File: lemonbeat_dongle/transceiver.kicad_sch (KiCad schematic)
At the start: 21 parts, among them J301 SMA, U301 Si4467, Y301 26MHz

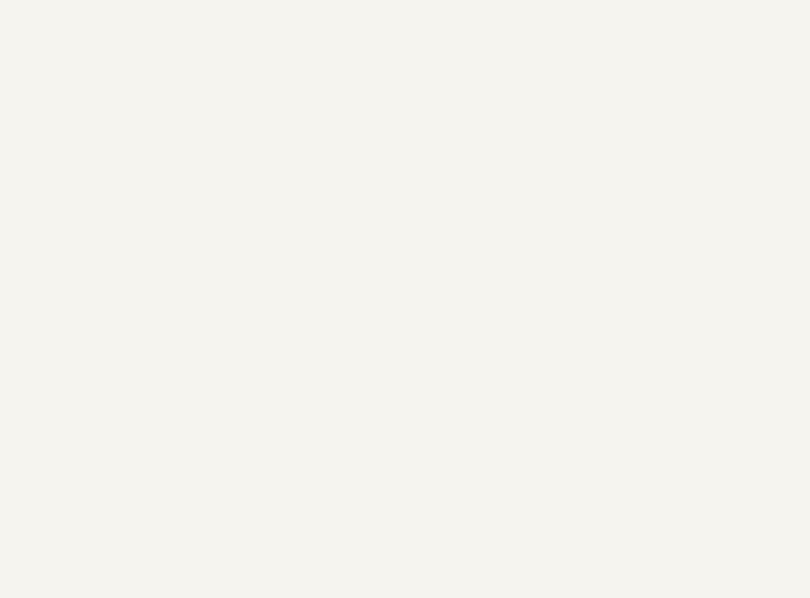
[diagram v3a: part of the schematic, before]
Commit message: dongle: add some LEDs
- power LED (connected to VBUS, constantly on if USB is powered)
- TX LED (GPIO2)
- RX LED (GPIO3)
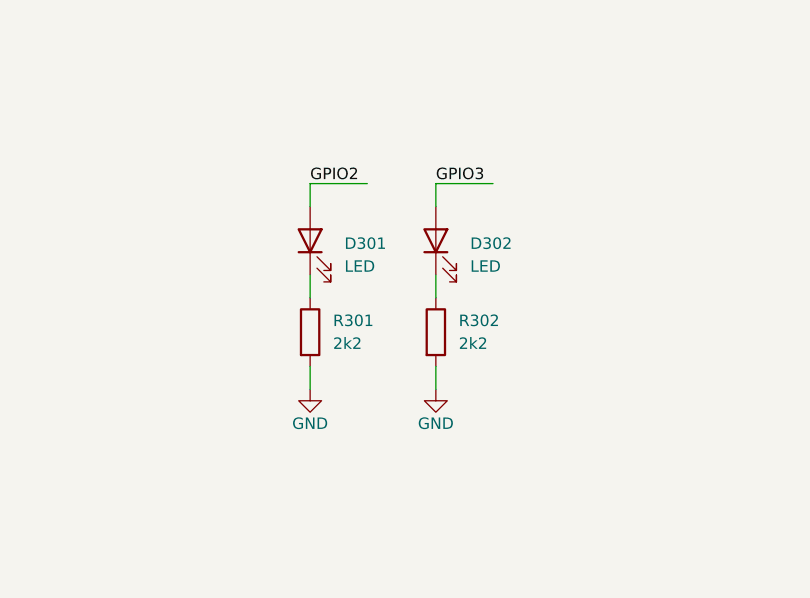
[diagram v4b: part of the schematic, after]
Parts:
- added D301, D302: LED, LED_SMD:LED_0805_2012Metric, symbol Device:LED
- added R301, R302: 2k2, Resistor_SMD:R_0402_1005Metric, symbol Device:R
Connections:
- net GND: now also R301.2, R302.2
- net GPIO2: now also D301.2 (A)
- net GPIO3: now also D302.2 (A)
- new net: D302.1 (K), R302.1
- new net: D301.1 (K), R301.1
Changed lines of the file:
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@@
+    (stroke (width 0) (type default) (color 0 0 0 0))
+  )
+  (wire (pts (xy 240.03 97.79) (xy 240.03 100.33))
     (stroke (width 0) (type default) (color 0 0 0 0))
   )
@@
     (stroke (width 0) (type default) (color 0 0 0 0))
   )
+  (wire (pts (xy 226.06 80.01) (xy 226.06 77.47))
+    (stroke (width 0) (type default) (color 0 0 0 0))
+  )
   (wire (pts (xy 82.55 81.28) (xy 83.82 81.28))
     (stroke (width 0) (type default) (color 0 0 0 0))
@@
     (stroke (width 0) (type default) (color 0 0 0 0))
   )
+  (wire (pts (xy 226.06 77.47) (xy 232.41 77.47))
+    (stroke (width 0) (type default) (color 0 0 0 0))
+  )
+  (wire (pts (xy 240.03 80.01) (xy 240.03 77.47))
+    (stroke (width 0) (type default) (color 0 0 0 0))
+  )
+  (wire (pts (xy 226.06 97.79) (xy 226.06 100.33))
+    (stroke (width 0) (type default) (color 0 0 0 0))
+  )
   (wire (pts (xy 91.44 111.76) (xy 96.52 111.76))
     (stroke (width 0) (type default) (color 0 0 0 0))
   )
+  (wire (pts (xy 240.03 77.47) (xy 246.38 77.47))
+    (stroke (width 0) (type default) (color 0 0 0 0))
+  )
   (wire (pts (xy 132.08 100.33) (xy 132.08 102.87))
     (stroke (width 0) (type default) (color 0 0 0 0))
@@
     (stroke (width 0) (type default) (color 0 0 0 0))
   )
+  (wire (pts (xy 226.06 87.63) (xy 226.06 90.17))
+    (stroke (width 0) (type default) (color 0 0 0 0))
+  )
   (wire (pts (xy 69.85 109.22) (xy 71.12 109.22))
     (stroke (width 0) (type default) (color 0 0 0 0))
@@
   )
   (wire (pts (xy 69.85 111.76) (xy 71.12 111.76))
+    (stroke (width 0) (type default) (color 0 0 0 0))
+  )
+  (wire (pts (xy 240.03 87.63) (xy 240.03 90.17))
     (stroke (width 0) (type default) (color 0 0 0 0))
   )
@@
     (effects (font (size 1.27 1.27)) (justify left bottom))
   )
+  (label "GPIO2" (at 226.06 77.47 0)
+    (effects (font (size 1.27 1.27)) (justify left bottom))
+  )
+  (label "GPIO3" (at 240.03 77.47 0)
+    (effects (font (size 1.27 1.27)) (justify left bottom))
+  )
   (hierarchical_label "MISO" (shape output) (at 69.85 109.22 180)
     (effects (font (size 1.27 1.27)) (justify right))
@@
     (pin "1")
   )
+  (symbol (lib_id "power:GND") (at 240.03 100.33 0) (unit 1)
+    (in_bom yes) (on_board yes)
+    (property "Reference" "#PWR0302" (id 0) (at 240.03 106.68 0)
+      (effects (font (size 1.27 1.27)) hide)
+    )
+    (property "Value" "GND" (id 1) (at 240.03 104.14 0))
+    (property "Footprint" "" (id 2) (at 240.03 100.33 0)
+      (effects (font (size 1.27 1.27)) hide)
+    )
+    (property "Datasheet" "" (id 3) (at 240.03 100.33 0)
+      (effects (font (size 1.27 1.27)) hide)
+    )
+    (pin "1")
+  )
+  (symbol (lib_id "Device:R") (at 240.03 93.98 0) (unit 1)
+    (in_bom yes) (on_board yes) (fields_autoplaced)
+    (property "Reference" "R302" (id 0) (at 242.57 92.7099 0)
+      (effects (font (size 1.27 1.27)) (justify left))
+    )
+    (property "Value" "2k2" (id 1) (at 242.57 95.2499 0)
+      (effects (font (size 1.27 1.27)) (justify left))
+    )
+    (property "Footprint" "Resistor_SMD:R_0402_1005Metric" (id 2) (at 238.252 93.98 90)
+      (effects (font (size 1.27 1.27)) hide)
+    )
+    (property "Datasheet" "https://datasheet.lcsc.com/lcsc/2206010045_UNI-ROYAL-Uniroyal-Elec-0402WGF2201TCE_C25879.pdf" (id 3) (at 240.03 93.98 0)
+      (effects (font (size 1.27 1.27)) hide)
+    )
+    (property "Comment" "JLCPCB basic part" (id 4) (at 240.03 93.98 0)
+      (effects (font (size 1.27 1.27)) hide)
+    )
+    (property "Description" "62.5mW Thick Film Resistors 50V ±100ppm/℃ ±1% -55℃~+155℃ 2.2kΩ 0402 Chip Resistor" (id 5) (at 240.03 93.98 0)
+      (effects (font (size 1.27 1.27)) hide)
+    )
+    (property "LCSC" "C25879" (id 6) (at 240.03 93.98 0)
+      (effects (font (size 1.27 1.27)) hide)
+    )
+    (property "Manufacturer" "Uniroyal Elec" (id 7) (at 240.03 93.98 0)
+      (effects (font (size 1.27 1.27)) hide)
+    )
+    (property "Part Number" "0402WGF2201TCE" (id 8) (at 240.03 93.98 0)
+      (effects (font (size 1.27 1.27)) hide)
+    )
+    (pin "1")
+    (pin "2")
+  )
   (symbol (lib_id "Device:C") (at 144.78 96.52 0) (unit 1)
     (in_bom yes) (on_board yes) (fields_autoplaced)
@@
     (pin "2")
   )
+  (symbol (lib_id "Device:LED") (at 226.06 83.82 90) (unit 1)
+    (in_bom yes) (on_board yes) (fields_autoplaced)
+    (property "Reference" "D301" (id 0) (at 229.87 84.1374 90)
+      (effects (font (size 1.27 1.27)) (justify right))
+    )
+    (property "Value" "LED" (id 1) (at 229.87 86.6774 90)
+      (effects (font (size 1.27 1.27)) (justify right))
+    )
+    (property "Footprint" "LED_SMD:LED_0805_2012Metric" (id 2) (at 226.06 83.82 0)
+      (effects (font (size 1.27 1.27)) hide)
+    )
+    (property "Datasheet" "https://datasheet.lcsc.com/lcsc/2008201032_Foshan-NationStar-Optoelectronics-NCD0805R1_C84256.pdf" (id 3) (at 226.06 83.82 0)
+      (effects (font (size 1.27 1.27)) hide)
+    )
+    (property "Comment" "JLCPCB basic part" (id 4) (at 226.06 83.82 0)
+      (effects (font (size 1.27 1.27)) hide)
+    )
+    (property "Description" "Red 0805 Light Emitting Diodes (LED) ROHS" (id 5) (at 226.06 83.82 0)
+      (effects (font (size 1.27 1.27)) hide)
+    )
+    (property "LCSC" "C84256" (id 6) (at 226.06 83.82 0)
+      (effects (font (size 1.27 1.27)) hide)
+    )
+    (property "Manufacturer" "Foshan NationStar Optoelectronics" (id 7) (at 226.06 83.82 0)
+      (effects (font (size 1.27 1.27)) hide)
+    )
+    (property "Part Number" "NCD0805R1" (id 8) (at 226.06 83.82 0)
+      (effects (font (size 1.27 1.27)) hide)
+    )
+    (pin "1")
+    (pin "2")
+  )
   (symbol (lib_id "Device:C") (at 113.03 46.99 0) (unit 1)
     (in_bom yes) (on_board yes) (fields_autoplaced)
@@
     (pin "2")
   )
+  (symbol (lib_id "Device:LED") (at 240.03 83.82 90) (unit 1)
+    (in_bom yes) (on_board yes) (fields_autoplaced)
+    (property "Reference" "D302" (id 0) (at 243.84 84.1374 90)
+      (effects (font (size 1.27 1.27)) (justify right))
+    )
+    (property "Value" "LED" (id 1) (at 243.84 86.6774 90)
+      (effects (font (size 1.27 1.27)) (justify right))
+    )
+    (property "Footprint" "LED_SMD:LED_0805_2012Metric" (id 2) (at 240.03 83.82 0)
+      (effects (font (size 1.27 1.27)) hide)
+    )
+    (property "Datasheet" "https://datasheet.lcsc.com/lcsc/2008201032_Foshan-NationStar-Optoelectronics-NCD0805R1_C84256.pdf" (id 3) (at 240.03 83.82 0)
+      (effects (font (size 1.27 1.27)) hide)
+    )
+    (property "Comment" "JLCPCB basic part" (id 4) (at 240.03 83.82 0)
+      (effects (font (size 1.27 1.27)) hide)
+    )
+    (property "Description" "Red 0805 Light Emitting Diodes (LED) ROHS" (id 5) (at 240.03 83.82 0)
+      (effects (font (size 1.27 1.27)) hide)
+    )
+    (property "LCSC" "C84256" (id 6) (at 240.03 83.82 0)
+      (effects (font (size 1.27 1.27)) hide)
+    )
+    (property "Manufacturer" "Foshan NationStar Optoelectronics" (id 7) (at 240.03 83.82 0)
+      (effects (font (size 1.27 1.27)) hide)
+    )
+    (property "Part Number" "NCD0805R1" (id 8) (at 240.03 83.82 0)
+      (effects (font (size 1.27 1.27)) hide)
+    )
+    (pin "1")
+    (pin "2")
+  )
   (symbol (lib_id "power:VDD") (at 97.79 146.05 0) (unit 1)
     (in_bom yes) (on_board yes)
@@
     (pin "1")
     (pin "2")
+  )
+  (symbol (lib_id "power:GND") (at 226.06 100.33 0) (unit 1)
+    (in_bom yes) (on_board yes)
+    (property "Reference" "#PWR0301" (id 0) (at 226.06 106.68 0)
+      (effects (font (size 1.27 1.27)) hide)
+    )
+    (property "Value" "GND" (id 1) (at 226.06 104.14 0))
+    (property "Footprint" "" (id 2) (at 226.06 100.33 0)
+      (effects (font (size 1.27 1.27)) hide)
+    )
+    (property "Datasheet" "" (id 3) (at 226.06 100.33 0)
+      (effects (font (size 1.27 1.27)) hide)
+    )
+    (pin "1")
   )
   (symbol (lib_id "Device:L") (at 115.57 88.9 90) (unit 1)
@@
     (pin "1")
   )
+  (symbol (lib_id "Device:R") (at 226.06 93.98 0) (unit 1)
+    (in_bom yes) (on_board yes) (fields_autoplaced)
+    (property "Reference" "R301" (id 0) (at 228.6 92.7099 0)
+      (effects (font (size 1.27 1.27)) (justify left))
+    )
+    (property "Value" "2k2" (id 1) (at 228.6 95.2499 0)
+      (effects (font (size 1.27 1.27)) (justify left))
+    )
+    (property "Footprint" "Resistor_SMD:R_0402_1005Metric" (id 2) (at 224.282 93.98 90)
+      (effects (font (size 1.27 1.27)) hide)
+    )
+    (property "Datasheet" "https://datasheet.lcsc.com/lcsc/2206010045_UNI-ROYAL-Uniroyal-Elec-0402WGF2201TCE_C25879.pdf" (id 3) (at 226.06 93.98 0)
+      (effects (font (size 1.27 1.27)) hide)
+    )
+    (property "Comment" "JLCPCB basic part" (id 4) (at 226.06 93.98 0)
+      (effects (font (size 1.27 1.27)) hide)
+    )
+    (property "Description" "62.5mW Thick Film Resistors 50V ±100ppm/℃ ±1% -55℃~+155℃ 2.2kΩ 0402 Chip Resistor" (id 5) (at 226.06 93.98 0)
+      (effects (font (size 1.27 1.27)) hide)
+    )
+    (property "LCSC" "C25879" (id 6) (at 226.06 93.98 0)
+      (effects (font (size 1.27 1.27)) hide)
+    )
+    (property "Manufacturer" "Uniroyal Elec" (id 7) (at 226.06 93.98 0)
+      (effects (font (size 1.27 1.27)) hide)
+    )
+    (property "Part Number" "0402WGF2201TCE" (id 8) (at 226.06 93.98 0)
+      (effects (font (size 1.27 1.27)) hide)
+    )
+    (pin "1")
+    (pin "2")
+  )
   (symbol (lib_id "power:GND") (at 120.65 76.2 0) (unit 1)

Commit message: dongle: schematic: add manufacturer & part number for SMA connector
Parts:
- J301: Manufacturer (none) -> Johnson; Part Number (none) -> 142-0701-851
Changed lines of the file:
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@@
+      (effects (font (size 1.27 1.27)) hide)
+    )
+    (property "Manufacturer" "Johnson" (id 4) (at 176.53 88.9 0)
+      (effects (font (size 1.27 1.27)) hide)
+    )
+    (property "Part Number" "142-0701-851" (id 5) (at 176.53 88.9 0)
       (effects (font (size 1.27 1.27)) hide)
     )

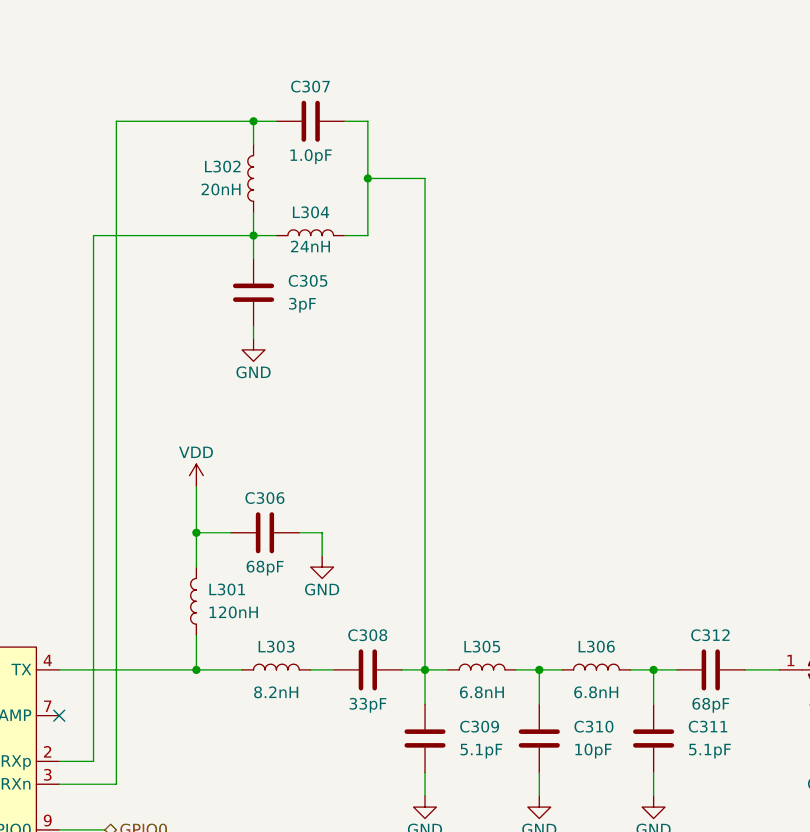
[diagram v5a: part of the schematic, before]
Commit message: dongle: update schematics & PCBs to KiCAD 7 & fix ERC/DRC errors & warnings
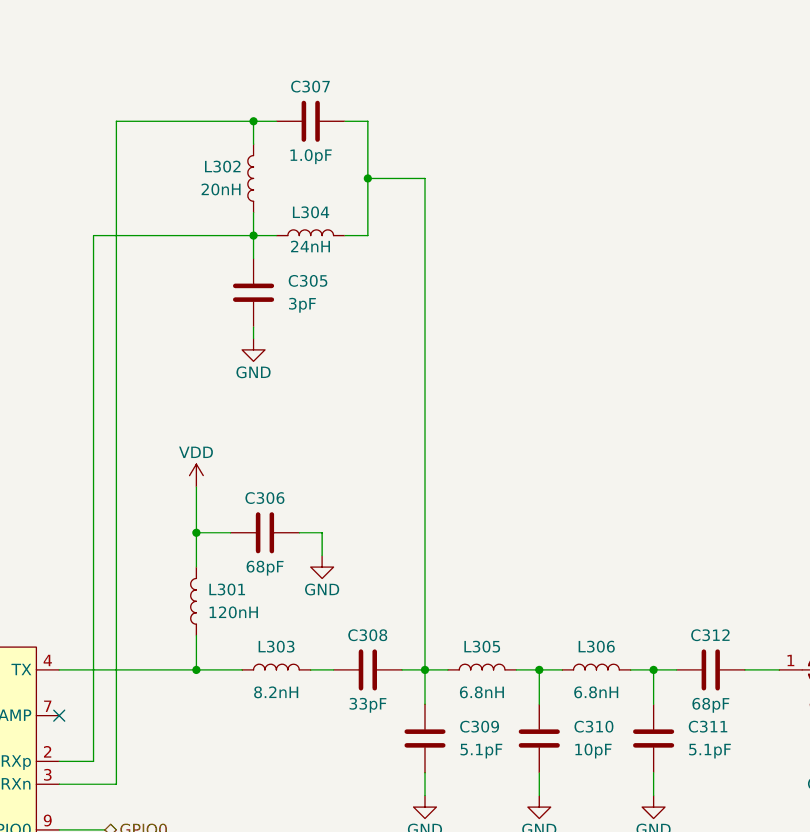
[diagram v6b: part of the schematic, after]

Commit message: dongle: BOM: add LCSC part number for SMA connector
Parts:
- J301: LCSC (none) -> C9900004170
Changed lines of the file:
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@@
+      (effects (font (size 1.27 1.27)) hide)
+    )
+    (property "LCSC" "C9900004170" (at 176.53 88.9 0)
       (effects (font (size 1.27 1.27)) hide)
     )

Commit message: dongle: add note regarding alternative model for SMA connector
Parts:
- J301: Comment (none) -> Alternative suitable part: Amphenol RF 901-10309
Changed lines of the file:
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@@
+      (effects (font (size 1.27 1.27)) hide)
+    )
+    (property "Comment" "Alternative suitable part: Amphenol RF 901-10309" (at 176.53 88.9 0)
       (effects (font (size 1.27 1.27)) hide)
     )
